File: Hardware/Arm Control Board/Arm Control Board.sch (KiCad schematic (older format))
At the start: 34 parts, among them P1 Servo 1, P10 UIM240XX_Stepper_Conn, P11 Battery, P12 SyRen, P13 Raspberry Pi, P14 Gripper Force Fdbk, P2 Shoulder Feedback, P3 Servo 2, P4 Servo 3, P5 Elbow Feedback, P6 Servo 4, P7 RS485, P8 ST_SWD_Connector, P9 Servo 5, U1 STM32F401RCT6, U2 SN75176BDR, U3 74LVCH244APW, X1 24MHz

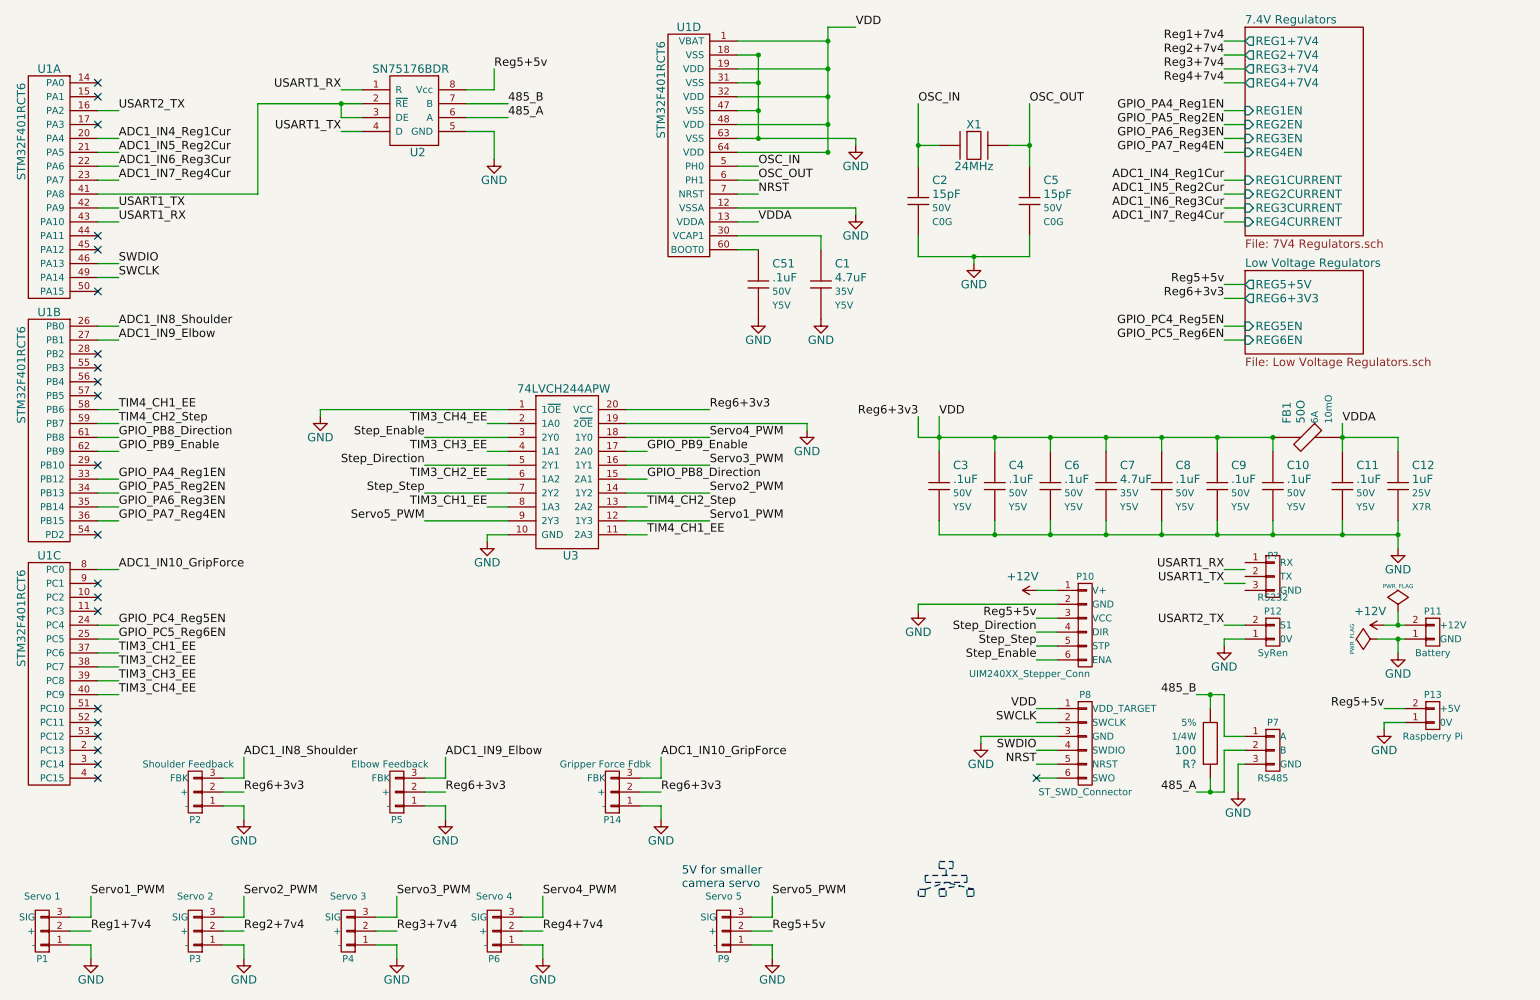
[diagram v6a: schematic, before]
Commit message: Improved serial and servo connectors, moved refs
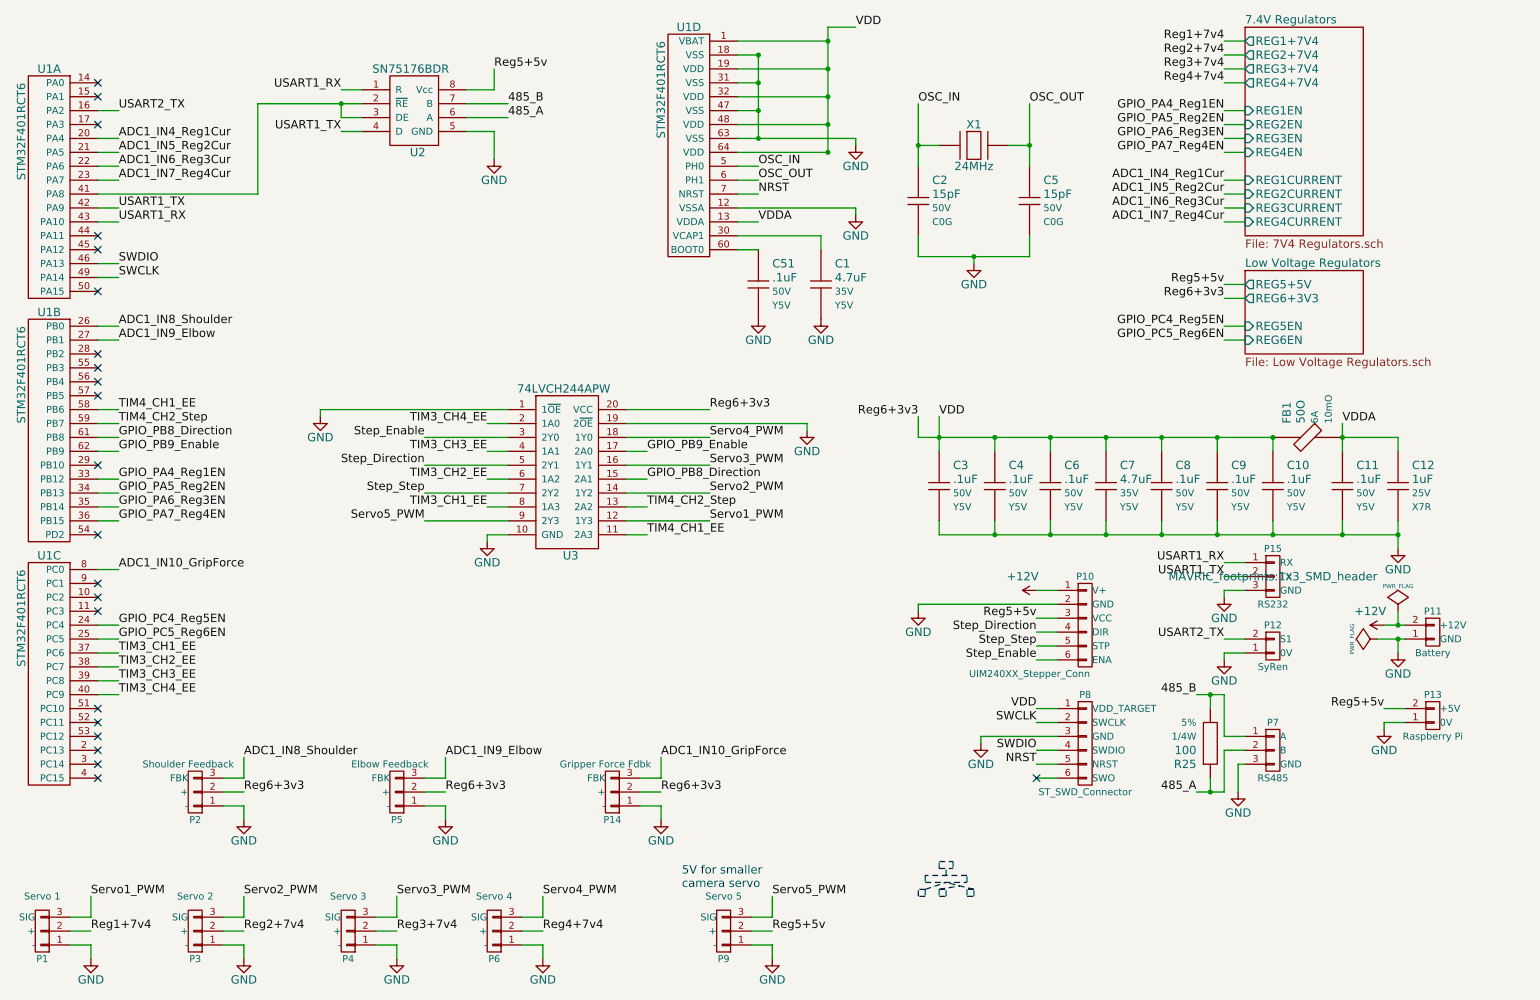
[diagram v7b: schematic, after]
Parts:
- removed P?: RS232, symbol RS232
- added P15: RS232, MAVRIC_footprints:1x3_SMD_header, symbol RS232
- P7: footprint MAVRIC_footprints:1x2_SMD_header -> MAVRIC_footprints:1x3_SMD_header
- gave numbers to parts that had none: 1
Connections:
- net GND: now also P15.3 (GND)
- net USART1_RX: now also P15.1 (RX)
- net USART1_TX: now also P15.2 (TX)
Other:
- moved on the sheet: P12
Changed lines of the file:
@@
 F 0 "P7" H 9650 6050 50  0000 C CNN
 F 1 "RS485" H 9650 5650 50  0000 C CNN
-F 2 "MAVRIC_footprints:1x2_SMD_header" H 9650 5850 60  0001 C CNN
+F 2 "MAVRIC_footprints:1x3_SMD_header" H 9650 5850 60  0001 C CNN
 F 3 "" H 9650 5850 60  0000 C CNN
 	1    9650 5850
@@
 L SYREN P12
 U 1 1 54C9E181
-P 9650 5000
-F 0 "P12" H 9650 5150 50  0000 C CNN
-F 1 "SyRen" H 9650 4850 50  0000 C CNN
-F 2 "MAVRIC_footprints:1x2_SMD_header" H 9650 5000 60  0001 C CNN
-F 3 "" H 9650 5000 60  0000 C CNN
-	1    9650 5000
+P 9650 5100
+F 0 "P12" H 9650 5250 50  0000 C CNN
+F 1 "SyRen" H 9650 4950 50  0000 C CNN
+F 2 "MAVRIC_footprints:1x2_SMD_header" H 9650 5100 60  0001 C CNN
+F 3 "" H 9650 5100 60  0000 C CNN
+	1    9650 5100
 	1    0    0    -1
 $EndComp
@@
 L GND #PWR09
 U 1 1 54C9E250
-P 9300 5100
-F 0 "#PWR09" H 9300 4850 60  0001 C CNN
-F 1 "GND" H 9300 4950 60  0000 C CNN
-F 2 "" H 9300 5100 60  0000 C CNN
-F 3 "" H 9300 5100 60  0000 C CNN
-	1    9300 5100
+P 9300 5200
+F 0 "#PWR09" H 9300 4950 60  0001 C CNN
+F 1 "GND" H 9300 5050 60  0000 C CNN
+F 2 "" H 9300 5200 60  0000 C CNN
+F 3 "" H 9300 5200 60  0000 C CNN
+	1    9300 5200
 	1    0    0    -1
 $EndComp
@@
 Text Label 1350 1250 0    60   ~ 0
 USART2_TX
-Text Label 9300 4950 2    60   ~ 0
+Text Label 9300 5050 2    60   ~ 0
 USART2_TX
 Text Label 9300 2600 2    60   ~ 0
@@
 ADC1_IN10_GripForce
 $Comp
-L GND #PWR?
+L GND #PWR028
 U 1 1 54E4E142
 P 9400 6150
-F 0 "#PWR?" H 9400 5900 60  0001 C CNN
+F 0 "#PWR028" H 9400 5900 60  0001 C CNN
 F 1 "GND" H 9400 6000 60  0000 C CNN
 F 2 "" H 9400 6150 60  0000 C CNN
@@
 485_A
 $Comp
-L Resistor R?
+L Resistor R25
 U 1 1 54E522EE
 P 9200 5800
-F 0 "R?" V 9050 5900 60  0000 L CNN
+F 0 "R25" V 9050 5900 60  0000 L CNN
 F 1 "100" V 9150 5900 60  0000 L CNN
 F 2 "Resistors_SMD:R_1206_HandSoldering" H 9100 5800 60  0001 C CNN
@@
 	0    -1   -1   0
 $EndComp
-Text Label 9300 4650 2    60   ~ 0
+Text Label 9300 4600 2    60   ~ 0
 USART1_TX
-Text Label 9300 4550 2    60   ~ 0
+Text Label 9300 4500 2    60   ~ 0
 USART1_RX
-$Comp
-L RS232 P?
-U 1 1 54E5BB0C
-P 9650 4600
-F 0 "P?" H 9650 4750 50  0000 C CNN
-F 1 "RS232" H 9650 4450 50  0000 C CNN
-F 2 "" H 9650 4600 60  0000 C CNN
-F 3 "" H 9650 4600 60  0000 C CNN
-	1    9650 4600
-	1    0    0    -1
-$EndComp
 Wire Wire Line
 	4150 1200 3850 1200
@@
 	4050 1400 4050 1600
 Wire Wire Line
-	10450 4950 10550 4950
-Wire Wire Line
-	10550 4950 10600 4950
-Wire Wire Line
-	10400 5050 10550 5050
-Wire Wire Line
-	10550 5050 10600 5050
+	10450 4950 10600 4950
+Wire Wire Line
+	10400 5050 10600 5050
 Wire Wire Line
 	1000 7250 1150 7250
@@
 	2350 1850 1200 1850
 Wire Wire Line
-	2350 1200 2950 1200
-Wire Wire Line
-	2950 1200 3100 1200
-Wire Wire Line
-	9450 5050 9300 5050
-Wire Wire Line
-	9300 5050 9300 5100
+	2350 1200 3100 1200
+Wire Wire Line
+	9450 5150 9300 5150
+Wire Wire Line
+	9300 5150 9300 5200
 Wire Wire Line
 	10450 5550 10600 5550
@@
 Connection ~ 5950 1050
 Wire Wire Line
-	5800 1450 5950 1450
-Wire Wire Line
-	5950 1450 6650 1450
+	5800 1450 6650 1450
 Connection ~ 5950 1450
 Wire Wire Line
@@
 	9650 3600 9650 3700
 Wire Wire Line
-	7250 3450 7250 3600
-Wire Wire Line
-	7250 3600 7250 3700
+	7250 3450 7250 3700
 Connection ~ 7250 3600
 Wire Wire Line
@@
 Connection ~ 5950 850
 Wire Wire Line
-	10150 3500 10150 3600
-Wire Wire Line
-	10150 3600 10150 3700
+	10150 3500 10150 3700
 Connection ~ 9650 3600
 Connection ~ 10150 3600
@@
 	10550 3600 10550 3700
 Wire Wire Line
-	10550 4200 10550 4300
-Wire Wire Line
-	10550 4300 10550 4400
+	10550 4200 10550 4400
 Wire Wire Line
 	10150 4300 10150 4200
@@
 	10150 3600 10550 3600
 Wire Wire Line
-	7250 4300 7650 4300
-Wire Wire Line
-	7650 4300 8050 4300
-Wire Wire Line
-	8050 4300 8450 4300
-Wire Wire Line
-	8450 4300 8850 4300
-Wire Wire Line
-	8850 4300 9250 4300
-Wire Wire Line
-	9250 4300 9650 4300
-Wire Wire Line
-	9650 4300 10150 4300
-Wire Wire Line
-	10150 4300 10550 4300
-Wire Wire Line
-	7100 3600 7250 3600
-Wire Wire Line
-	7250 3600 7650 3600
-Wire Wire Line
-	7650 3600 8050 3600
-Wire Wire Line
-	8050 3600 8450 3600
-Wire Wire Line
-	8450 3600 8850 3600
-Wire Wire Line
-	8850 3600 9250 3600
-Wire Wire Line
-	9250 3600 9650 3600
+	7250 4300 10550 4300
+Wire Wire Line
+	7100 3600 9650 3600
 Wire Wire Line
 	9450 750  9300 750
@@
 	1200 1250 1350 1250
 Wire Wire Line
-	9450 4950 9300 4950
+	9450 5050 9300 5050
 Wire Wire Line
 	5000 3400 5600 3400
@@
 	5800 1750 5950 1750
 Wire Wire Line
-	7100 1200 7100 1500
-Wire Wire Line
-	7100 1500 7100 1650
+	7100 1200 7100 1650
 Wire Wire Line
 	7100 1500 7250 1500
@@
 	7750 1500 7900 1500
 Wire Wire Line
-	7900 1200 7900 1500
-Wire Wire Line
-	7900 1500 7900 1650
+	7900 1200 7900 1650
 Wire Wire Line
 	7100 2150 7100 2300
 Wire Wire Line
-	7100 2300 7500 2300
-Wire Wire Line
-	7500 2300 7900 2300
+	7100 2300 7900 2300
 Wire Wire Line
 	7900 2300 7900 2150
@@
 	9450 1750 9300 1750
 Wire Wire Line
-	5950 850  5950 1050
-Wire Wire Line
-	5950 1050 5950 1250
-Wire Wire Line
-	5950 1250 5950 1450
-Wire Wire Line
-	6450 650  6450 750
-Wire Wire Line
-	6450 750  6450 950
-Wire Wire Line
-	6450 950  6450 1150
-Wire Wire Line
-	6450 1150 6450 1350
-Wire Wire Line
-	6450 1350 6450 1550
+	5950 850  5950 1450
+Wire Wire Line
+	6450 650  6450 1550
 Wire Wire Line
 	5800 2250 5950 2250
@@
 	9300 5850 9300 6150
 Wire Wire Line
-	9300 6150 9200 6150
-Wire Wire Line
-	9200 6150 9100 6150
-Wire Wire Line
-	9100 5450 9200 5450
-Wire Wire Line
-	9200 5450 9300 5450
+	9300 6150 9100 6150
+Wire Wire Line
+	9100 5450 9300 5450
 Wire Wire Line
 	9300 5450 9300 5750
 Wire Wire Line
-	9450 4550 9300 4550
-Wire Wire Line
-	9300 4650 9450 4650
+	9450 4500 9300 4500
+Wire Wire Line
+	9300 4600 9450 4600
 Wire Wire Line
 	9200 5550 9200 5450
@@
 	9200 6050 9200 6150
 Connection ~ 9200 6150
+$Comp
+L RS232 P15
+U 1 1 54E5727F
+P 9650 4600
+F 0 "P15" H 9650 4800 50  0000 C CNN
+F 1 "RS232" H 9650 4400 50  0000 C CNN
+F 2 "MAVRIC_footprints:1x3_SMD_header" H 9650 4600 60  0000 C CNN
+F 3 "" H 9650 4600 60  0000 C CNN
+	1    9650 4600
+	1    0    0    -1
+$EndComp
+$Comp
+L GND #PWR029
+U 1 1 54E57350
+P 9300 4750
+F 0 "#PWR029" H 9300 4500 60  0001 C CNN
+F 1 "GND" H 9300 4600 60  0000 C CNN
+F 2 "" H 9300 4750 60  0000 C CNN
+F 3 "" H 9300 4750 60  0000 C CNN
+	1    9300 4750
+	1    0    0    -1
+$EndComp
+Wire Wire Line
+	9450 4700 9300 4700
+Wire Wire Line
+	9300 4700 9300 4750
 $EndSCHEMATC

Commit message: Add cat5 jack for ethernet
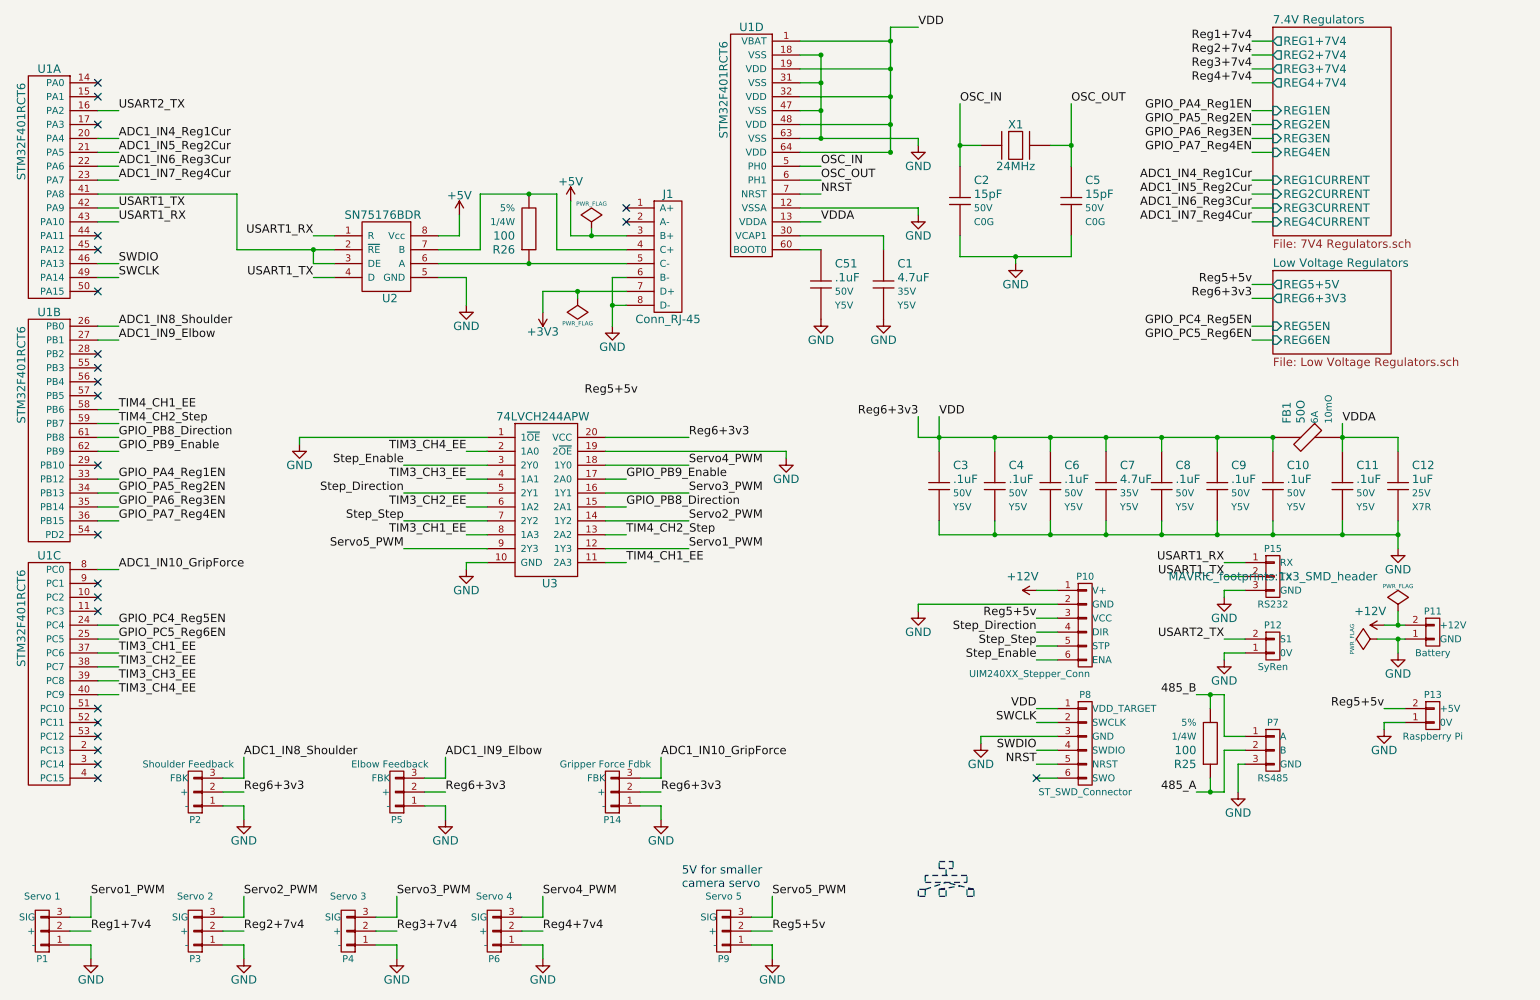
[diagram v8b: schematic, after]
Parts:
- added J1: Conn_RJ-45, symbol Conn_RJ-45
- added R26: 100, Resistors_SMD:R_1206_HandSoldering, symbol Resistor
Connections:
- net 485_A: no longer U2.6 (A)
- net 485_B: no longer U2.7 (B)
- net GND: now also J1.6 (B-), J1.8 (D-)
- net Reg5+5v: no longer U2.8 (Vcc)
- new net: J1.5 (C-), R26.1, U2.6 (A)
- new net: J1.4 (C+), R26.2, U2.7 (B)
- new net +3V3: J1.7 (D+)
- new net +5V: J1.3 (B+), U2.8 (Vcc)
- no-connect marks 22 -> 24
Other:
- moved on the sheet: C1, C2, C5, C51, U1D, U2, U3, X1
